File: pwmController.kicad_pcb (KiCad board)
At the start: 2 copper layers, 100 x 100 mm, 67 parts, among them J201 track out, J202 track out, J301 relays, J302 relays, J401 inputs, J402 inputs, J403 common, J501 power, J601 Conn_01x06_Male, J602 RJ12, J603 RJ12, J604 Conn_01x06_Female, J801 ADC, J802 ADC, K301 G5V-1, K302 G5V-1, K303 G5V-1, K304 G5V-1, K305 G5V-1, K306 G5V-1, K307 G5V-1, K308 G5V-1, M801 Motor_Servo, M802 Motor_Servo, M803 Motor_Servo, M804 Motor_Servo, M805 Motor_Servo, M806 Motor_Servo, M807 Motor_Servo, M808 Motor_Servo, U201 L298N, U301 PCF8574, U302 ULN2803A, U401 MCP23017_SP, U501 Buck, U601 MAX485E, U701 24LC256

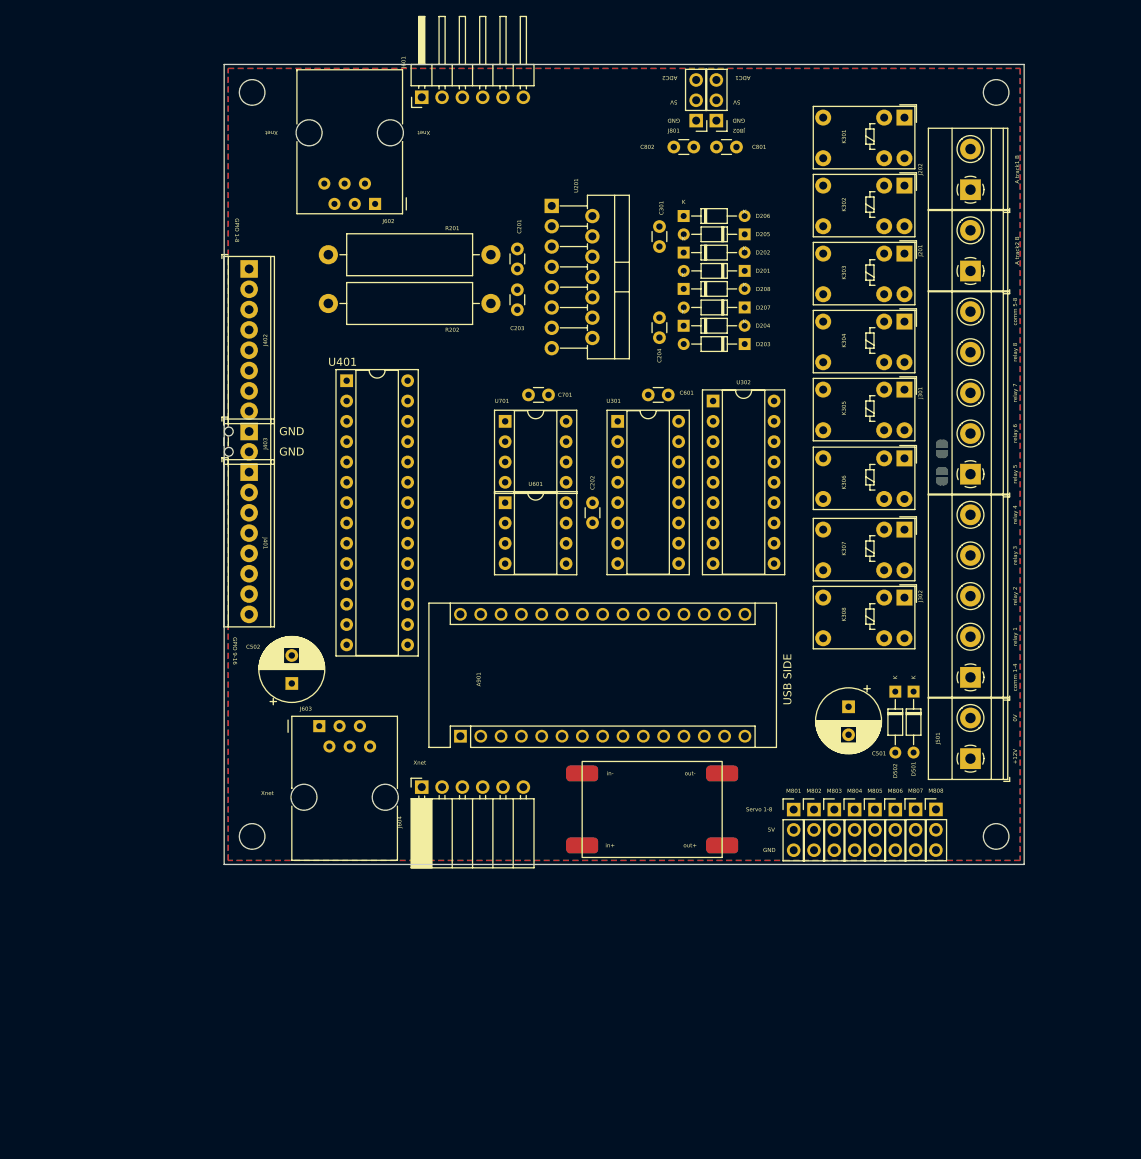
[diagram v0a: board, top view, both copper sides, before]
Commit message: altered the code drastically and made a new PCB. PCB is still much work.
I finally fixed that issue where loco functions and speed were not serviced to the multimaus clients.
The Nx code also has been succesfully tested using the monitor.
MCP bug also has been solded. The bug was in assembleIO.py
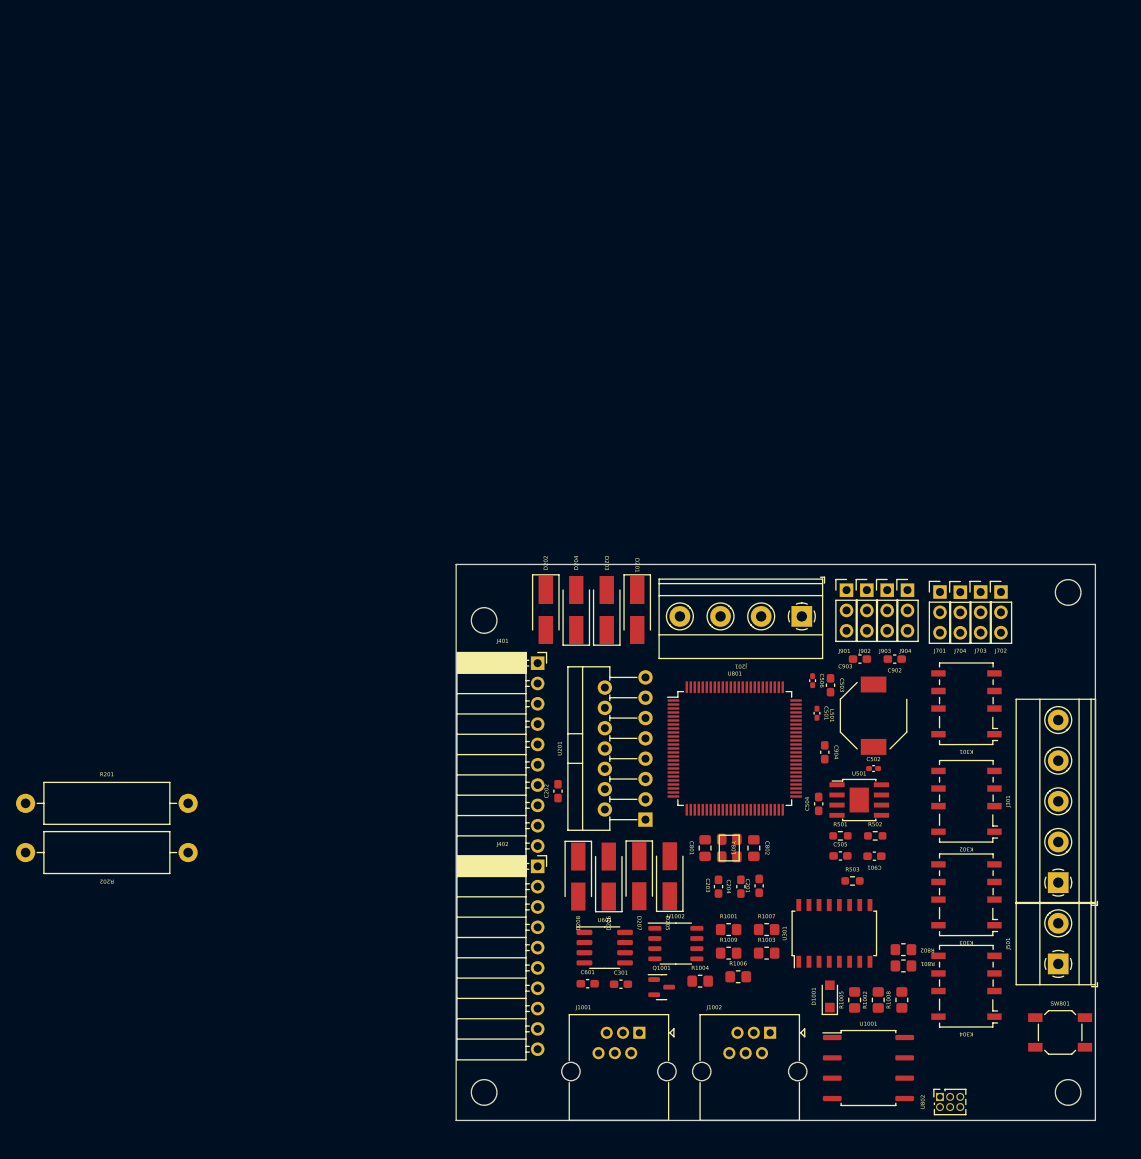
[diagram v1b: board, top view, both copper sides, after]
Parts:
- removed A901: Arduino_Nano_v3.x, Module:Arduino_Nano
- removed C701: 100nF, Capacitor_THT:C_Disc_D3.0mm_W1.6mm_P2.50mm
- removed D501, D502: D, Diode_THT:D_DO-34_SOD68_P7.62mm_Horizontal
- removed J202: track out, TerminalBlock_Phoenix:TerminalBlock_Phoenix_MKDS-1,5-2-5.08_1x02_P5.08mm_Horizontal
- removed J302: relays, TerminalBlock_Phoenix:TerminalBlock_Phoenix_MKDS-1,5-5-5.08_1x05_P5.08mm_Horizontal
- removed J403: common, TerminalBlock_Phoenix:TerminalBlock_Phoenix_MPT-0,5-2-2.54_1x02_P2.54mm_Horizontal
- removed J601: Conn_01x06_Male, Connector_PinHeader_2.54mm:PinHeader_1x06_P2.54mm_Horizontal
- removed J602, J603: RJ12, Connector_RJ:RJ12_Amphenol_54601
- removed J604: Conn_01x06_Female, Connector_PinSocket_2.54mm:PinSocket_1x06_P2.54mm_Horizontal
- removed J801, J802: ADC, Connector_PinHeader_2.54mm:PinHeader_1x03_P2.54mm_Vertical
- removed JP301, JP302: jmp, Jumper:SolderJumper-2_P1.3mm_Open_RoundedPad1.0x1.5mm
- removed K305, K306, K307, K308: G5V-1, Relay_THT:Relay_SPDT_Omron_G5V-1
- removed M801, M802, M803, M804, M805, M806, M807, M808: Motor_Servo, Connector_PinHeader_2.54mm:PinHeader_1x03_P2.54mm_Vertical
- removed the REF** at (71.5, 122.5)
- removed the REF** at (71.5, 29.5)
- removed the REF** at (164.5, 29.5)
- removed the REF** at (164.5, 122.5)
- removed U302: ULN2803A, Package_DIP:DIP-18_W7.62mm_Socket
- removed U401: MCP23017_SP, Package_DIP:DIP-28_W7.62mm_Socket
- removed U701: 24LC256, Package_DIP:DIP-8_W7.62mm_Socket
- added C503: 22uF, Capacitor_SMD:C_0603_1608Metric_Pad1.08x0.95mm_HandSolder, F.Cu at (143.8, 103.6)
- added C504: 22uF, Capacitor_SMD:C_0603_1608Metric_Pad1.08x0.95mm_HandSolder, F.Cu at (142.3, 118.4)
- added C505: 22uF, Capacitor_SMD:C_0603_1608Metric_Pad1.08x0.95mm_HandSolder, F.Cu at (145.0, 124.9)
- added C506: 100nF, Capacitor_SMD:C_0402_1005Metric_Pad0.74x0.62mm_HandSolder, F.Cu at (141.6, 103.0)
- added C901: 100nF, Capacitor_SMD:C_0603_1608Metric_Pad1.08x0.95mm_HandSolder, F.Cu at (149.3, 125.0)
- added C902: 100nF, Capacitor_SMD:C_0603_1608Metric_Pad1.08x0.95mm_HandSolder, F.Cu at (151.8, 100.3)
- added C903: 100nF, Capacitor_SMD:C_0603_1608Metric_Pad1.08x0.95mm_HandSolder, F.Cu at (147.5, 100.3)
- added C904: 100nF, Capacitor_SMD:C_0603_1608Metric_Pad1.08x0.95mm_HandSolder, F.Cu at (143.1, 112.0)
- added D1001: D, Diode_SMD:Nexperia_CFP3_SOD-123W, F.Cu at (143.7, 142.5)
- added J1001: RJ12, Connector_RJ:RJ25_Wayconn_MJEA-660X1_Horizontal, F.Cu at (119.9, 147.0)
- added J1002: RJ12, Connector_RJ:RJ25_Wayconn_MJEA-660X1_Horizontal, F.Cu at (136.2, 147.0)
- added J701: Conn_01x03_Male, Connector_PinHeader_2.54mm:PinHeader_1x03_P2.54mm_Vertical, F.Cu at (157.5, 91.9)
- added J702: Conn_01x03_Male, Connector_PinHeader_2.54mm:PinHeader_1x03_P2.54mm_Vertical, F.Cu at (165.1, 91.9)
- added J703: Conn_01x03_Male, Connector_PinHeader_2.54mm:PinHeader_1x03_P2.54mm_Vertical, F.Cu at (162.6, 91.9)
- added J704: Conn_01x03_Male, Connector_PinHeader_2.54mm:PinHeader_1x03_P2.54mm_Vertical, F.Cu at (160.0, 92.0)
- added J901: ADC, Connector_PinHeader_2.54mm:PinHeader_1x03_P2.54mm_Vertical, F.Cu at (145.8, 91.7)
- added J902: ADC, Connector_PinHeader_2.54mm:PinHeader_1x03_P2.54mm_Vertical, F.Cu at (148.3, 91.7)
- added J903: ADC, Connector_PinHeader_2.54mm:PinHeader_1x03_P2.54mm_Vertical, F.Cu at (150.9, 91.7)
- added J904: ADC, Connector_PinHeader_2.54mm:PinHeader_1x03_P2.54mm_Vertical, F.Cu at (153.4, 91.7)
- added L501: L, Inductor_SMD:L_Bourns-SRU8028_8.0x8.0mm, F.Cu at (149.2, 107.4)
- added Q1001: AO3400A, Package_TO_SOT_SMD:SOT-23, F.Cu at (122.7, 141.3)
- added R1001: 10k, Resistor_SMD:R_0805_2012Metric_Pad1.20x1.40mm_HandSolder, F.Cu at (131.1, 134.1)
- added R1002: 10k, Resistor_SMD:R_0805_2012Metric_Pad1.20x1.40mm_HandSolder, F.Cu at (149.8, 142.9)
- added R1003: 1k, Resistor_SMD:R_0805_2012Metric_Pad1.20x1.40mm_HandSolder, F.Cu at (135.8, 137.1)
- added R1004: 220k, Resistor_SMD:R_0805_2012Metric_Pad1.20x1.40mm_HandSolder, F.Cu at (127.5, 140.6)
- added R1005: 47k, Resistor_SMD:R_0805_2012Metric_Pad1.20x1.40mm_HandSolder, F.Cu at (146.8, 142.9)
- added R1006: 10k, Resistor_SMD:R_0805_2012Metric_Pad1.20x1.40mm_HandSolder, F.Cu at (132.2, 140.0)
- added R1007: 150k, Resistor_SMD:R_0805_2012Metric_Pad1.20x1.40mm_HandSolder, F.Cu at (135.8, 134.1)
- added R1008: 22k, Resistor_SMD:R_0805_2012Metric_Pad1.20x1.40mm_HandSolder, F.Cu at (152.7, 142.9)
- added R1009: 10k, Resistor_SMD:R_0805_2012Metric_Pad1.20x1.40mm_HandSolder, F.Cu at (131.1, 137.1)
- added R501: 220k, Resistor_SMD:R_0603_1608Metric_Pad0.98x0.95mm_HandSolder, F.Cu at (145.0, 122.4)
- added R502: 150k, Resistor_SMD:R_0603_1608Metric_Pad0.98x0.95mm_HandSolder, F.Cu at (149.4, 122.4)
- added R503: 20k, Resistor_SMD:R_0603_1608Metric_Pad0.98x0.95mm_HandSolder, F.Cu at (146.5, 128.1)
- added R801: 10k, Resistor_SMD:R_0805_2012Metric_Pad1.20x1.40mm_HandSolder, F.Cu at (152.9, 138.7)
- added R802: 10k, Resistor_SMD:R_0805_2012Metric_Pad1.20x1.40mm_HandSolder, F.Cu at (152.9, 136.7)
- added REF**: MountingHole_3.2mm_M3, MountingHole:MountingHole_3.2mm_M3, F.Cu at (173.5, 92.0)
- added REF**: MountingHole_3.2mm_M3, MountingHole:MountingHole_3.2mm_M3, F.Cu at (100.5, 95.5)
- added REF**: MountingHole_3.2mm_M3, MountingHole:MountingHole_3.2mm_M3, F.Cu at (173.5, 154.5)
- added REF**: MountingHole_3.2mm_M3, MountingHole:MountingHole_3.2mm_M3, F.Cu at (100.5, 154.5)
- added SW801: SW_SPST, Button_Switch_SMD:SW_SPST_SKQG_WithStem, F.Cu at (172.5, 147.0)
- added U1001: 6N137, Package_SO:SOP-8_6.62x9.15mm_P2.54mm, F.Cu at (148.5, 151.4)
- added U1002: LM311, Package_SO:SOP-8_3.9x4.9mm_P1.27mm, F.Cu at (124.5, 135.9)
- added U801: ATmega2560-16A, Package_QFP:TQFP-100_14x14mm_P0.5mm, F.Cu at (131.8, 111.5)
- added U802: HEADER_3x2, Connector_PinSocket_1.27mm:PinSocket_2x03_P1.27mm_Vertical, F.Cu at (157.5, 155.1)
- added Y801: crystal_arduino, custom_kicad_lib_sk:crystal_arduino, F.Cu at (131.2, 124.0)
- C201, C202, C203, C204, C301, C601: footprint Capacitor_THT:C_Disc_D3.0mm_W1.6mm_P2.50mm -> Capacitor_SMD:C_0603_1608Metric_Pad1.08x0.95mm_HandSolder
- C501: value CP -> 100nF; footprint Capacitor_THT:CP_Radial_D8.0mm_P3.50mm -> Capacitor_SMD:C_0402_1005Metric_Pad0.74x0.62mm_HandSolder
- C502: value CP -> 22nF; footprint Capacitor_THT:CP_Radial_D8.0mm_P3.50mm -> Capacitor_SMD:C_0402_1005Metric_Pad0.74x0.62mm_HandSolder
- C801, C802: value 100nF -> 12pF; footprint Capacitor_THT:C_Disc_D3.0mm_W1.6mm_P2.50mm -> Capacitor_SMD:C_0805_2012Metric_Pad1.18x1.45mm_HandSolder
- D201, D202, D203, D204, D205, D206, D207, D208: footprint Diode_THT:D_DO-34_SOD68_P7.62mm_Horizontal -> Diode_SMD:D_SMA_Handsoldering
- J201: value track out -> Screw_Terminal_01x04; footprint TerminalBlock_Phoenix:TerminalBlock_Phoenix_MKDS-1,5-2-5.08_1x02_P5.08mm_Horizontal -> TerminalBlock_Phoenix:TerminalBlock_Phoenix_MKDS-1,5-4-5.08_1x04_P5.08mm_Horizontal
- J401, J402: value inputs -> Conn_01x10_Female; footprint TerminalBlock_Phoenix:TerminalBlock_Phoenix_MPT-0,5-8-2.54_1x08_P2.54mm_Horizontal -> Connector_PinSocket_2.54mm:PinSocket_1x10_P2.54mm_Horizontal
- K301, K302, K303, K304: value G5V-1 -> G6K-2; footprint Relay_THT:Relay_SPDT_Omron_G5V-1 -> Relay_SMD:Relay_DPDT_Omron_G6K-2F-Y
- U301: value PCF8574 -> ULN2003A; footprint Package_DIP:DIP-16_W7.62mm_Socket -> Package_SO:SOIC-16W_5.3x10.2mm_P1.27mm
- U501: value Buck -> MT2499A; footprint custom_kicad_lib_sk:Buck -> Package_SO:TI_SO-PowerPAD-8
- U601: value MAX485E -> 24LC256; footprint Package_DIP:DIP-8_W7.62mm_Socket -> Package_SO:SOP-8_3.76x4.96mm_P1.27mm
- moved C301 92.3 mm to (117.6, 141.0), turned to 0 degrees
- moved C802 88.2 mm to (134.2, 124.0), turned to -90 degrees
- moved C801 87.7 mm to (128.1, 124.0), turned to 90 degrees
- moved K304 83.4 mm to (160.8, 141.2), turned to 180 degrees
- moved D206 83.1 mm to (116.1, 127.5), turned to 90 degrees
- moved J402 82.9 mm to (107.2, 126.2), turned to 0 degrees
- moved C201 82.8 mm to (134.9, 128.7)
- moved D205 80.8 mm to (123.7, 127.5), turned to 90 degrees
- moved K303 80.5 mm to (160.8, 129.8), turned to 180 degrees
- moved R202 78.4 mm to (63.5, 124.5)
- moved R201 78.3 mm to (43.2, 118.4)
- moved U201 77.6 mm to (120.7, 120.4), turned to 90 degrees
- moved K302 77.4 mm to (160.8, 118.1), turned to 180 degrees
- moved C203 76.4 mm to (129.8, 128.8), turned to -90 degrees
- moved D208 74.6 mm to (112.3, 127.5), turned to -90 degrees
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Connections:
- C201 pad 2: CS1 -> +5V
- C202 pad 1: +5V -> +12V
- C203 pad 1: CS2 -> GND
- C203 pad 2: GND -> CS1
- C204 pad 1: +12V -> CS2
- C501 pad 1: +5VA -> Net-(C501-Pad1)
- C501 pad 2: GND -> Net-(C501-Pad2)
- C502 pad 1: +5V -> Net-(C501-Pad1)
- C502 pad 2: GND -> Net-(C501-Pad2)
- C801 pad 1: +5V -> GND
- C801 pad 2: ADC1 -> /uController/X1
- C802 pad 1: +5V -> GND
- C802 pad 2: ADC2 -> /uController/X2
- D202 pad 1: track1R -> +12V
- D202 pad 2: GND -> track1L
- D203 pad 1: +12V -> track1R
- D203 pad 2: track2R -> GND
- D204 pad 1: track2R -> track1L
- D205 pad 2: track1L -> track2R
- D206 pad 1: track1L -> +12V
- D206 pad 2: GND -> track2L
- D207 pad 1: +12V -> track2R
- D207 pad 2: track2L -> GND
- J401 pad 1: Net-(J401-Pad1) -> +5V
- J401 pad 2: Net-(J401-Pad2) -> GPIO1
- J401 pad 3: Net-(J401-Pad3) -> GPIO2
- J401 pad 4: Net-(J401-Pad4) -> GPIO3
- J401 pad 5: Net-(J401-Pad5) -> GPIO4
- J401 pad 6: Net-(J401-Pad6) -> GPIO5
- J401 pad 7: Net-(J401-Pad7) -> GPIO6
- J401 pad 8: Net-(J401-Pad8) -> GPIO7
- J402 pad 1: Net-(J402-Pad1) -> +5V
- J402 pad 2: Net-(J402-Pad2) -> GPIO9
- J402 pad 3: Net-(J402-Pad3) -> GPIO10
- J402 pad 4: Net-(J402-Pad4) -> GPIO11
- J402 pad 5: Net-(J402-Pad5) -> GPIO12
- J402 pad 6: Net-(J402-Pad6) -> GPIO13
- J402 pad 7: Net-(J402-Pad7) -> GPIO14
- J402 pad 8: Net-(J402-Pad8) -> GPIO15
- J501 pad 1: Net-(D501-Pad2) -> VCC
- K301 pad 1: unconnected-(K301-Pad1) -> +5V
- K301 pad 2: +5V -> unconnected-(K301-Pad2)
- K301 pad 5: Net-(J301-Pad5) -> unconnected-(K301-Pad5)
- K301 pad 6: Net-(J301-Pad5) -> unconnected-(K301-Pad6)
- K302 pad 1: unconnected-(K302-Pad1) -> +5V
- K302 pad 2: +5V -> unconnected-(K302-Pad2)
- K302 pad 5: Net-(J301-Pad5) -> unconnected-(K302-Pad5)
- K302 pad 6: Net-(J301-Pad5) -> unconnected-(K302-Pad6)
- K303 pad 1: unconnected-(K303-Pad1) -> +5V
- K303 pad 2: +5V -> unconnected-(K303-Pad2)
- K303 pad 5: Net-(J301-Pad5) -> unconnected-(K303-Pad5)
- K303 pad 6: Net-(J301-Pad5) -> unconnected-(K303-Pad6)
- K304 pad 1: unconnected-(K304-Pad1) -> +5V
- K304 pad 2: +5V -> unconnected-(K304-Pad2)
- K304 pad 5: Net-(J301-Pad5) -> unconnected-(K304-Pad5)
- K304 pad 6: Net-(J301-Pad5) -> unconnected-(K304-Pad6)
- U301 pad 1: +5V -> relay1
- U301 pad 10: Net-(U301-Pad10) -> unconnected-(U301-Pad10)
- U301 pad 11: Net-(U301-Pad11) -> unconnected-(U301-Pad11)
- U301 pad 12: Net-(U301-Pad12) -> unconnected-(U301-Pad12)
- U301 pad 13: unconnected-(U301-Pad13) -> /relays/coil4
- U301 pad 14: SCL -> /relays/coil3
- U301 pad 15: SDA -> /relays/coil2
- U301 pad 16: +5V -> /relays/coil1
- U301 pad 2: GND -> relay2
- U301 pad 3: GND -> relay3
- U301 pad 4: Net-(U301-Pad4) -> relay4
- U301 pad 5: Net-(U301-Pad5) -> unconnected-(U301-Pad5)
- U301 pad 6: Net-(U301-Pad6) -> unconnected-(U301-Pad6)
- U301 pad 7: Net-(U301-Pad7) -> unconnected-(U301-Pad7)
- U301 pad 9: Net-(U301-Pad9) -> +5V
- U501 pad 1: +5VA -> Net-(C501-Pad1)
- U501 pad 2: GND -> VCC
- U501 pad 3: GND -> Net-(C501-Pad2)
- U501 pad 4: Net-(D501-Pad1) -> GND
- U601 pad 1: Rx -> GND
- U601 pad 2: 485dir -> GND
- U601 pad 3: 485dir -> GND
- U601 pad 4: Tx -> GND
- U601 pad 5: GND -> SDA
- U601 pad 6: /interface/A -> SCL
- U601 pad 7: /interface/B -> GND
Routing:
- removed copper zone on B.Cu, net GND
- removed copper zone on F.Cu, net GND
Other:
- board size 100 x 100 mm -> 79.9 x 69.5 mm
- board text removed: "+12V"
- board text removed: "0V"
- board text removed: "5V"
- board text removed: "A track1 B"
- board text removed: "A track2 B"
- board text removed: "ADC1"
- board text removed: "ADC2"
- board text removed: "GND"
- board text removed: "GPIO 1-8"
- board text removed: "GPIO 9-16"
- board text removed: "Servo 1-8"
- board text removed: "USB SIDE"
- board text removed: "Xnet"
- board text removed: "comm 1-4"
- board text removed: "comm 5-8"
- board text removed: "relay 1"
- board text removed: "relay 2"
- board text removed: "relay 3"
- board text removed: "relay 4"
- board text removed: "relay 5"
- board text removed: "relay 6"
- board text removed: "relay 7"
- board text removed: "relay 8"

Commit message: replaced the atmega2560 by an stm32
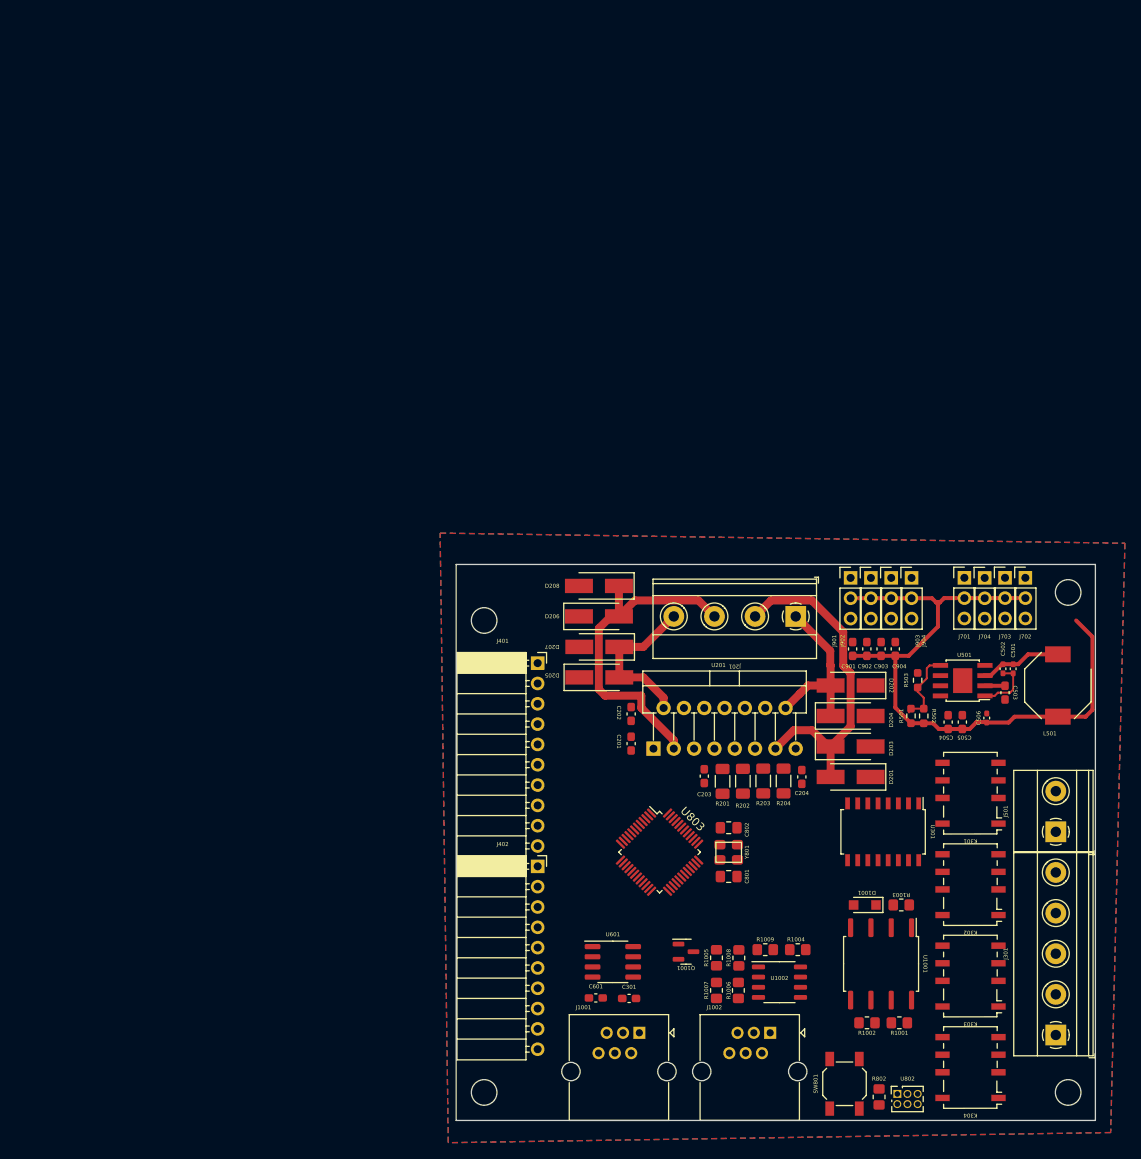
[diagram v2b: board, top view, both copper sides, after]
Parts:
- removed R801: 10k, Resistor_SMD:R_0805_2012Metric_Pad1.20x1.40mm_HandSolder
- removed U801: ATmega2560-16A, Package_QFP:TQFP-100_14x14mm_P0.5mm
- added R203: 0R01, Resistor_SMD:R_1206_3216Metric_Pad1.30x1.75mm_HandSolder, F.Cu at (135.4, 115.6)
- added R204: 0R01, Resistor_SMD:R_1206_3216Metric_Pad1.30x1.75mm_HandSolder, F.Cu at (137.9, 115.6)
- added U803: STM32F103C6Tx, Package_QFP:LQFP-48_7x7mm_P0.5mm, F.Cu at (122.4, 124.5)
- R201, R202: value R -> 0R01; footprint Resistor_THT:R_Axial_DIN0516_L15.5mm_D5.0mm_P20.32mm_Horizontal -> Resistor_SMD:R_1206_3216Metric_Pad1.30x1.75mm_HandSolder
- moved R201 87.2 mm to (130.3, 115.6), turned to 90 degrees
- moved R202 69.9 mm to (132.8, 115.6), turned to 90 degrees
- moved D202 39.3 mm to (146.3, 103.6), turned to 180 degrees
- moved D204 36.8 mm to (146.3, 107.4), turned to 0 degrees
- moved D208 36.4 mm to (114.8, 91.2), turned to 180 degrees
- moved D203 34.9 mm to (146.3, 111.3), turned to 0 degrees
- moved D201 33.9 mm to (146.3, 115.1), turned to 180 degrees
- moved D206 32.5 mm to (114.8, 95.0), turned to 0 degrees
- moved D207 29.1 mm to (114.9, 98.8), turned to 180 degrees
- moved SW801 27.7 mm to (145.5, 153.4), turned to 90 degrees
- moved R503 26.4 mm to (154.7, 103.0), turned to 90 degrees
- moved D205 26.4 mm to (114.9, 102.6), turned to 0 degrees
- moved C901 26.1 mm to (146.6, 99.1), turned to 90 degrees
- moved C501 25.1 mm to (166.6, 101.5), turned to 90 degrees
- moved R1001 24.3 mm to (152.4, 145.8), turned to 180 degrees
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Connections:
- J701 pad 2: +5VA -> +5V
- J702 pad 2: +5VA -> +5V
- J703 pad 2: +5VA -> +5V
- J704 pad 2: +5VA -> +5V
- R202 pad 1: CS2 -> GND
- R202 pad 2: GND -> CS1
- SW801 pad 2: Net-(SW801-Pad2) -> unconnected-(SW801-Pad2)
- U201 pad 13: track2R -> track1R
- U201 pad 14: track2L -> track1L
- U201 pad 2: track1R -> track2R
- U201 pad 3: track1L -> track2L
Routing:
- net +5V: track 0.00 -> 83.2 mm
- net track2L: track 0.00 -> 42.1 mm
- net track1R: track 0.00 -> 41.7 mm
- net track1L: track 0.00 -> 21.0 mm
- net track2R: track 0.00 -> 20.1 mm
- net Net-(C501-Pad2): track 0.00 -> 10.2 mm
- net Net-(R501-Pad2): track 0.00 -> 9.30 mm
- net Net-(C501-Pad1): track 0.00 -> 7.16 mm
- net VCC: track 0.00 -> 2.51 mm
- added copper zone on B.Cu, net GND
- added copper zone on F.Cu, net GND
